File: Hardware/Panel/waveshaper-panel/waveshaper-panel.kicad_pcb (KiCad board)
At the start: 2 copper layers, 100 x 200 mm, 24 parts

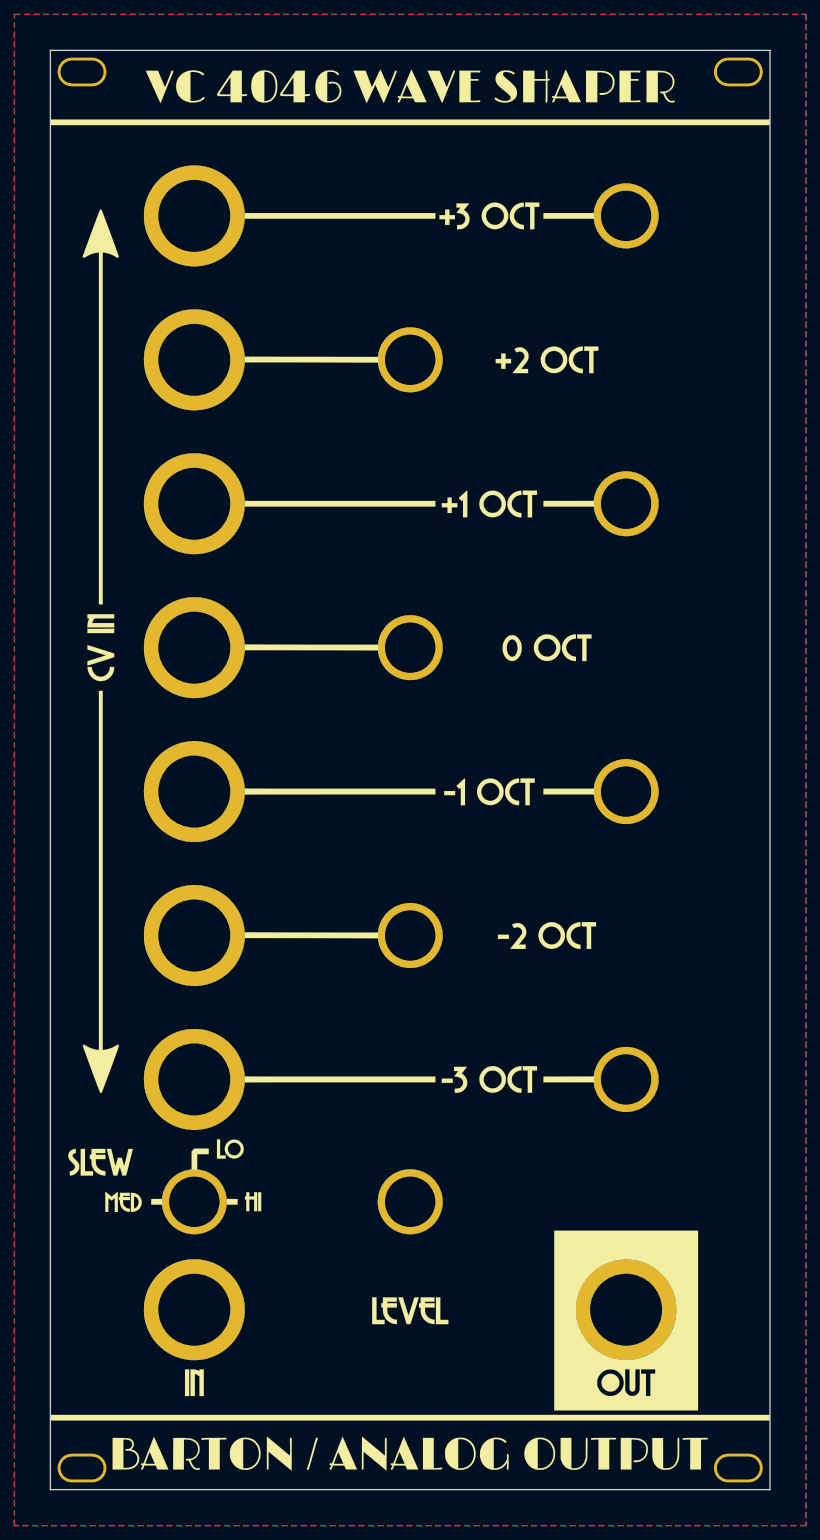
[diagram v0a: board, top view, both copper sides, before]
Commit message: PCB tweak, font correction on panel
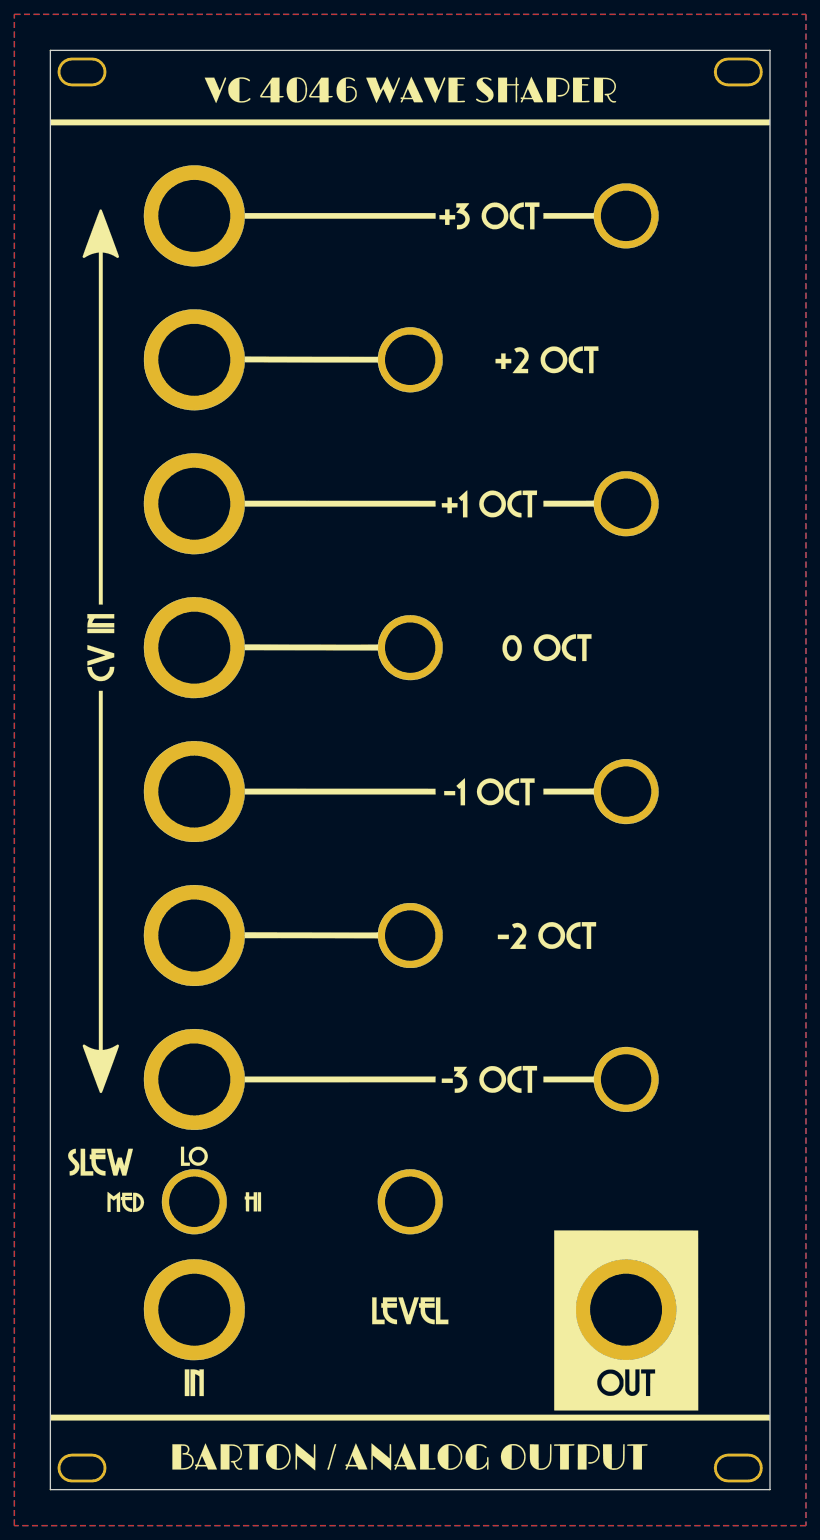
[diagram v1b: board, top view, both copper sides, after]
